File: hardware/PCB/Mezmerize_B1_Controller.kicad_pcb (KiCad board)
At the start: 2 copper layers, 100 x 70.9 mm, 51 parts, among them J1 230 Vac, J10 I2C DISPLAY (OLED/LCD), J11 I2C (FUTURE USE), J12 ROTARY ENC & SWITCH (FUTURE U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, J13 ROTARY ENC & SWITCH, J14 IR RECV, J2 B1 Relays, J3 PWR AMP L 12V TRIGGER, J4 PWR AMP L SWITCH, J5 PWR AMP R 12V TRIGGER, J6 PWR AMP R SWITCH, J7 PWR AMP TEMP NTC L, J8 PWR AMP TEMP NTC R, J9 MUSES 72320 (SPI), U1 AGQ20T03, U2 AGQ20T03, U3 ULN2803ADWR, U4 L7808CV, U5 MCP23008-E_SO, U6 24C02C_SN, U8 ESP32-DEVKIT-V1

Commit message: schenatics + symbols
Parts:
- moved U8 25.5 mm to (116.8, 172.7), turned to -90 degrees

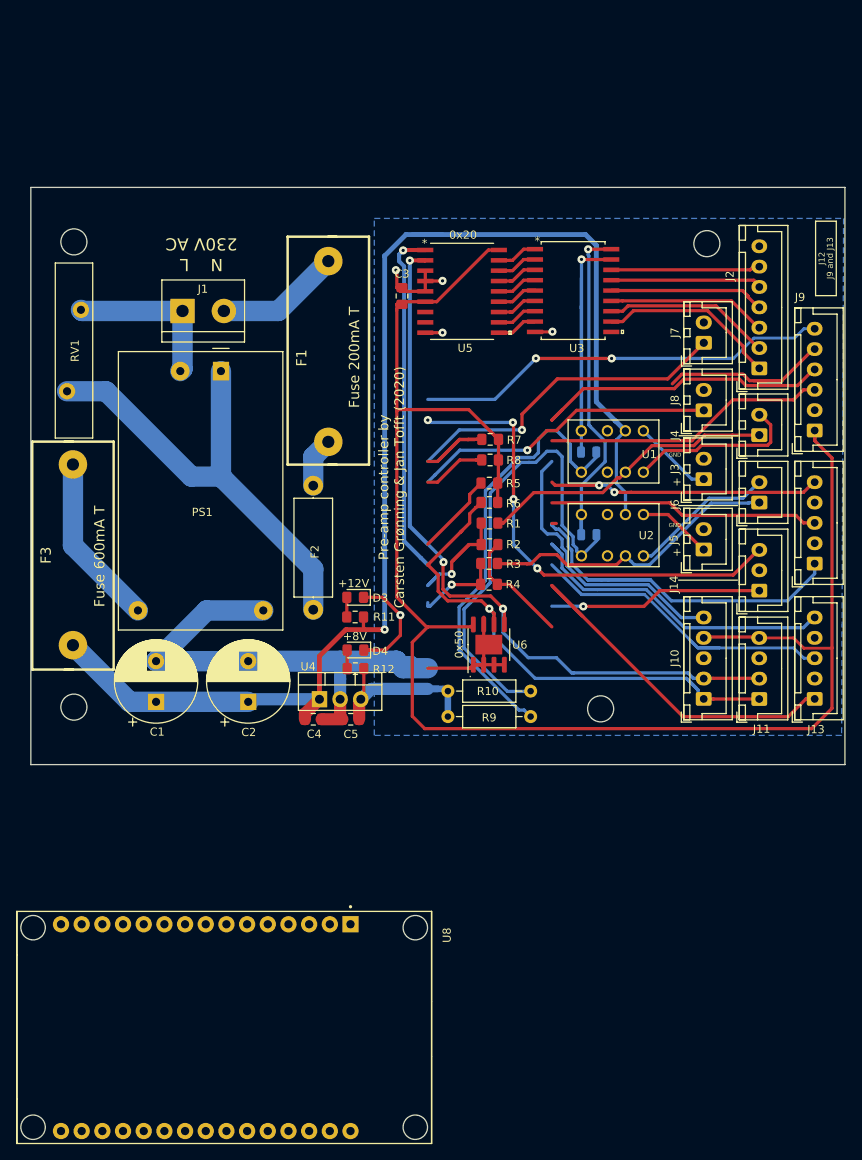
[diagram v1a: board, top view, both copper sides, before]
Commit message: PCB split
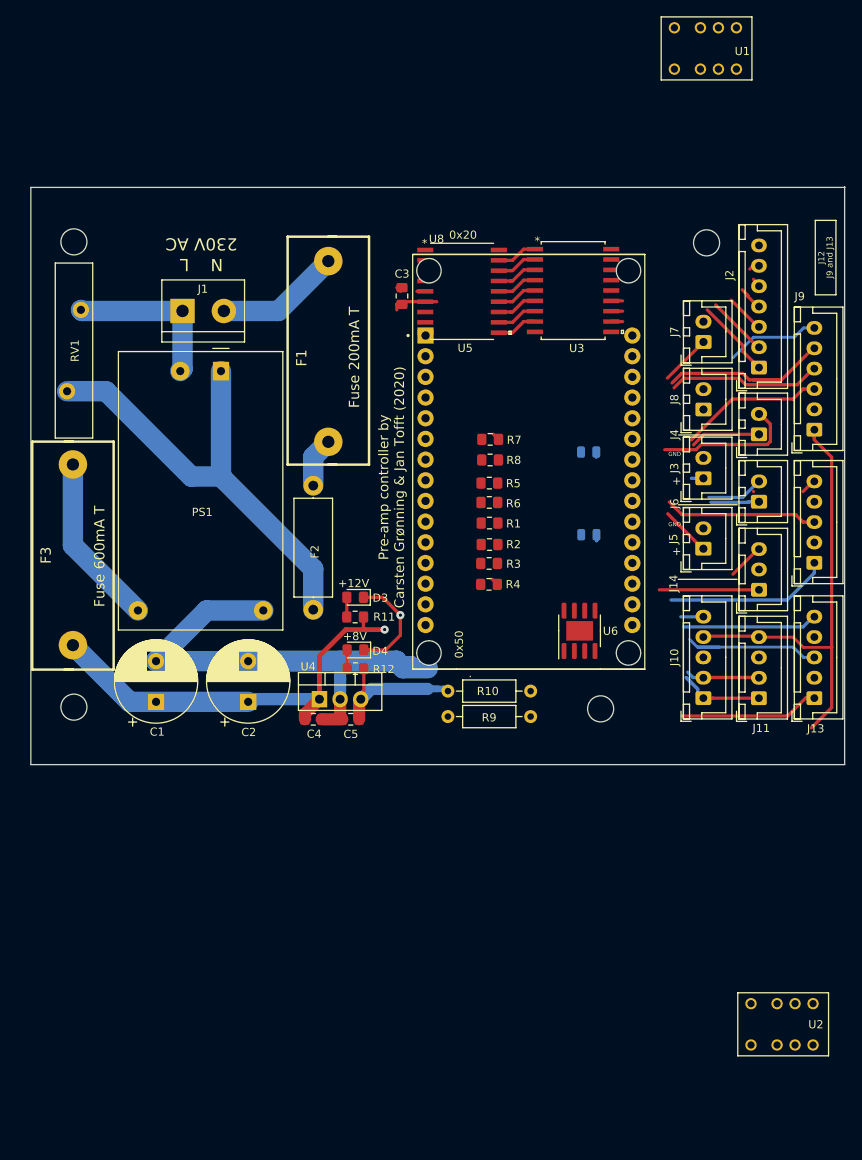
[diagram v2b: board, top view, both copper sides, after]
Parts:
- moved U8 78.9 mm to (154.3, 103.2), turned to 0 degrees
- moved U2 63.6 mm to (189.4, 169.8)
- moved U1 50.8 mm to (180.0, 49.9)
- moved U6 11.3 mm to (160.5, 124.0)
- moved J3 0.11 mm to (175.7, 105.2)
- moved J14 0.11 mm to (182.5, 118.9)
- moved J9 0.11 mm to (189.3, 99.3)
- moved REF** 0.11 mm to (176.1, 76.3)
- moved J10 0.11 mm to (175.7, 132.2)
- moved J5 0.11 mm to (175.7, 113.9)
- moved J11 0.11 mm to (182.5, 132.2)
- moved J12 0.11 mm to (189.3, 115.6)
- moved J13 0.11 mm to (189.3, 132.2)
- moved J2 0.11 mm to (182.5, 91.6)
- moved J4 0.11 mm to (182.5, 99.8)
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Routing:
- net +3V3: track 262.4 -> 67.2 mm, vias 4 -> 0
- net +12V: track 166.3 -> 53.2 mm
- net I2C:SCL: track 108.6 -> 12.0 mm, vias 2 -> 0
- net I2C:SDA: track 101.5 -> 9.18 mm, vias 3 -> 0
- net Net-(D1-Pad1): track 62.7 -> 0.63 mm
- net Net-(D2-Pad1): track 58.9 -> 1.38 mm
- net NTC_L: track 56.9 -> 6.26 mm, vias 1 -> 0
- net Net-(D1-Pad2): track 46.4 -> 0.05 mm, vias 1 -> 0
- net NTC_R: track 69.4 -> 24.1 mm, vias 1 -> 0
- net GND: track 160.5 -> 115.8 mm, vias 5 -> 1
- net Net-(D2-Pad2): track 42.5 -> 0.13 mm, vias 1 -> 0
- net Net-(J9-Pad6): track 51.1 -> 11.5 mm, vias 2 -> 0
- net Net-(U8-Pad22): track 34.7 -> 2.70 mm
- net Net-(J6-Pad1): track 38.1 -> 6.22 mm
- net Net-(U8-Pad23): track 33.5 -> 1.91 mm, vias 2 -> 0
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- removed copper zone on B.Cu, net GND
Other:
- board size 100 x 70.9 mm -> 100 x 71 mm

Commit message: Missing changes ??
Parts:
- removed the C1 at (108.5, 132.7)
- removed C2: 470uF, Capacitor_THT:CP_Radial_D10.0mm_P5.00mm
- removed C4: 0.33uF, Capacitor_SMD:C_0805_2012Metric_Pad1.15x1.40mm_HandSolder
- removed C5: 0.1uF, Capacitor_SMD:C_0805_2012Metric_Pad1.15x1.40mm_HandSolder
- removed D3, D4: LED, LED_SMD:LED_0805_2012Metric_Pad1.15x1.40mm_HandSolder
- removed F1: Fuse 200mA T, B1 Mezmerize Controller:BLX-A
- removed F2: Thermal fuse 73dgr, Resistor_THT:R_Axial_DIN0414_L11.9mm_D4.5mm_P15.24mm_Horizontal
- removed F3: Fuse 600mA T, B1 Mezmerize Controller:BLX-A
- removed the J1 at (111.7, 84.7)
- removed PS1: HLK-PM12, Converter_ACDC:Converter_ACDC_HiLink_HLK-PMxx
- removed the R1 at (149.4, 110.7)
- removed R11, R12: 4K7, Resistor_SMD:R_0805_2012Metric_Pad1.15x1.40mm_HandSolder
- removed R2: 5K, Resistor_SMD:R_0805_2012Metric_Pad1.15x1.40mm_HandSolder
- removed R3: 10K, Resistor_SMD:R_0805_2012Metric_Pad1.15x1.40mm_HandSolder
- removed the R4 at (149.4, 118.3)
- removed REF** (x4): MountingHole_3.2mm_M3_ISO7380, MountingHole:MountingHole_3.2mm_M3_ISO7380
- removed RV1: Varistor, Varistor:RV_Disc_D21.5mm_W4.6mm_P10mm
- removed the U4 at (128.5, 132.4)
- removed U8: ESP32-DEVKIT-V1, Dev Kit 1 - esp32:MODULE_ESP32_DEVKIT_V1
- added J14: 12V, TerminalBlock:TerminalBlock_bornier-2_P5.08mm, F.Cu at (175.8, 120.4)
- added J15: 8V, TerminalBlock:TerminalBlock_bornier-2_P5.08mm, F.Cu at (175.8, 108.9)
- added U6: ESP32-DEVKIT-V1, ESP32FP:MODULE_ESP32_DEVKIT_V1, F.Cu at (230.4, 114.1)
- D1, D2: moved to F.Cu
- J11: renamed from J12; value ROTARY ENC & SWITCH (FUTURE USE) -> ROTARY ENC & SWITCH 1
- J12: renamed from J13; value ROTARY ENC & SWITCH -> ROTARY ENC & SWITCH 2
- moved R7 103.8 mm to (252.6, 112.6)
- moved R9 103.8 mm to (252.4, 121.5), turned to 180 degrees
- moved R8 102.6 mm to (252.0, 106.4)
- moved C1 99.4 mm to (233.2, 113.6), turned to -90 degrees
- moved J6 93.3 mm to (262.3, 123.3), turned to -90 degrees
- moved J7 87.9 mm to (261.9, 113.9), turned to -90 degrees
- moved U4 85.9 mm to (225.8, 114.2), turned to 180 degrees
- moved R10 84.5 mm to (233.9, 106.5), turned to 180 degrees
- moved U5 83.7 mm to (243.5, 113.6), turned to -90 degrees
- moved J13 81.2 mm to (262.0, 102.2), turned to -90 degrees
- moved J9 77.5 mm to (253.2, 133.8), turned to 180 degrees
- moved U1 76.4 mm to (188.4, 125.8), turned to 0 degrees
- moved U2 69.2 mm to (183.2, 100.9), turned to 180 degrees
- moved U3 61.5 mm to (212.1, 114.3), turned to 180 degrees
- moved R1 59.5 mm to (201.5, 117.9), turned to 180 degrees
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- renumbered C3 to C1, J2 to J1, J11 to J10, J14 to J13, J3 to J2, J4 to J3, J5 to J4, J6 to J5, J7 to J6, J8 to J7, J9 to J8, J10 to J9, R9 to R1, R5 to R10, R10 to R4, R6 to R9, U5 to U4, U6 to U5
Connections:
- J11 pad 1: Net-(U8-Pad25) -> SW_1
- J11 pad 3: Net-(U8-Pad24) -> CCW_1
- J11 pad 5: Net-(U8-Pad23) -> CW_1
- J12 pad 1: Net-(J13-Pad1) -> SW_2
- J12 pad 3: Net-(J13-Pad3) -> CCW_2
- J12 pad 5: Net-(J13-Pad5) -> CW_2
- J13 pad 1: Net-(J14-Pad1) -> IR OUT
- J8 pad 3: Net-(J9-Pad3) -> SPI:SS
- J8 pad 4: Net-(J9-Pad4) -> SPI:MOSI
- J8 pad 5: NTC_R -> SPI:MISO
- J8 pad 6: Net-(J9-Pad6) -> SPI:SCK
- J9 pad 5: Net-(U8-Pad22) -> CONTRAST(LCD)
- R9 pad 1: I2C:SCL -> SPI:MOSI
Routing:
- net GND: track 115.8 -> 1.67 mm, vias 1 -> 0
- net Net-(F1-Pad2): track 64.6 -> 0.00 mm
- net +3V3: track 67.2 -> 5.71 mm
- net +12V: track 53.2 -> 0.00 mm, vias 1 -> 0
- net NTC_R: track 24.1 -> 0.00 mm
- net Net-(F3-Pad2): track 21.2 -> 0.00 mm
- net Net-(U8-Pad25): track 20.2 -> 0.00 mm
- net Net-(J1-Pad1) (its old number): track 20.0 -> 0.00 mm
- net Net-(J9-Pad4): track 19.0 -> 0.00 mm
- net +8V: track 18.9 -> 0.00 mm
- net Net-(J13-Pad3): track 18.9 -> 0.00 mm
- net Net-(U8-Pad24): track 18.8 -> 0.00 mm
- net Net-(J9-Pad3): track 17.7 -> 0.00 mm
- net Net-(J3-Pad2): track 17.4 -> 0.00 mm
- net Net-(J13-Pad1): track 17.1 -> 0.00 mm
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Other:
- board outline removed
- board text removed: "+"
- board text removed: "+12V"
- board text removed: "+8V"
- board text removed: "."
- board text removed: "0x50"
- board text removed: "230V AC"
- board text removed: "GND"
- board text removed: "J9 and J13"
- board text removed: "N L"

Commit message: mod psu + control v 0.25
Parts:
- added REF**: MountingHole_3.2mm_M3_ISO7380, MountingHole:MountingHole_3.2mm_M3_ISO7380, F.Cu at (125.0, 55.0)
- added REF**: MountingHole_3.2mm_M3_ISO7380, MountingHole:MountingHole_3.2mm_M3_ISO7380, F.Cu at (175.0, 145.0)
- added REF**: MountingHole_3.2mm_M3_ISO7380, MountingHole:MountingHole_3.2mm_M3_ISO7380, F.Cu at (175.0, 55.0)
- added REF**: MountingHole_3.2mm_M3_ISO7380, MountingHole:MountingHole_3.2mm_M3_ISO7380, F.Cu at (125.0, 145.0)
- moved J6 124.4 mm to (139.9, 145.5), turned to 180 degrees
- moved J9 123.9 mm to (129.3, 136.4), turned to 90 degrees
- moved J7 116.9 mm to (149.3, 145.1), turned to 180 degrees
- moved R9 111.6 mm to (141.7, 135.6), turned to 90 degrees
- moved J13 109.8 mm to (161.0, 145.2), turned to 180 degrees
- moved J8 108.1 mm to (129.3, 119.8), turned to 90 degrees
- moved R7 104.7 mm to (150.6, 135.8), turned to 90 degrees
- moved R8 99.5 mm to (156.8, 135.2), turned to -90 degrees
- moved U5 94.8 mm to (149.6, 126.7), turned to 180 degrees
- moved J10 93.9 mm to (128.8, 99.1), turned to 90 degrees
- moved J3 91.1 mm to (125.0, 65.5), turned to 90 degrees
- moved J2 90.9 mm to (125.0, 75.5), turned to 90 degrees
- moved C1 83.6 mm to (149.6, 116.4), turned to 180 degrees
- moved U6 81.3 mm to (149.1, 113.6), turned to 0 degrees
- moved J11 80.8 mm to (169.2, 126.4), turned to -90 degrees
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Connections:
- J14 pad 1: GND -> +12V
- J14 pad 2: +12V -> GND
- J15 pad 1: GND -> +8V
- J15 pad 2: +8V -> GND
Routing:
- net +12V: track 0.00 -> 67.7 mm
- net +8V: track 0.00 -> 52.0 mm
- net Net-(J3-Pad1): track 0.00 -> 17.0 mm
- net Net-(J4-Pad1): track 0.00 -> 16.6 mm
- net Net-(J3-Pad2): track 0.00 -> 14.4 mm
- net Net-(J5-Pad1): track 0.00 -> 13.7 mm
- net Net-(J5-Pad2): track 0.00 -> 9.76 mm
- net Net-(J2-Pad1): track 0.00 -> 9.76 mm
- net Net-(D2-Pad1): track 0.00 -> 8.58 mm
- net Net-(D1-Pad1): track 0.00 -> 6.72 mm
- net Net-(D2-Pad2): track 0.00 -> 3.94 mm
- net Net-(D1-Pad2): track 0.00 -> 3.74 mm
- net Net-(J1-Pad3): track 1.39 -> 0.00 mm
- net Net-(J1-Pad2): track 1.39 -> 0.00 mm
- net Net-(J1-Pad1): track 1.39 -> 0.00 mm
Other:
- board outline added: 60 x 100 mm

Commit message: updated pcb
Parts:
- moved J8 10.6 mm to (125.0, 110.0)
- moved R7 10.4 mm to (153.8, 126.0)
- moved J9 10.2 mm to (125.0, 127.2)
- moved R9 10.1 mm to (144.8, 126.0), turned to -90 degrees
- moved J10 9.53 mm to (125.0, 90.3)
- moved R8 9.30 mm to (158.0, 126.0)
- moved U5 7.39 mm to (150.6, 119.4)
- moved J11 7.30 mm to (175.0, 122.0)
- moved J1 7.28 mm to (175.0, 82.7)
- moved J12 6.99 mm to (175.0, 104.8)
- moved R10 6.50 mm to (150.6, 114.8), turned to 0 degrees
- moved J13 4.36 mm to (162.6, 141.2)
- moved C1 4.34 mm to (150.6, 112.2)
- moved U3 4.34 mm to (149.9, 91.1)
- moved U4 4.34 mm to (150.0, 104.8)
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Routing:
- net +3V3: track 5.71 -> 138.4 mm
- net CONTRAST(LCD): track 0.00 -> 98.9 mm
- net I2C:SDA: track 0.16 -> 78.6 mm, vias 0 -> 3
- net I2C:SCL: track 0.06 -> 76.1 mm, vias 0 -> 1
- net NTC_L: track 0.00 -> 65.6 mm
- net SPI:MOSI: track 0.00 -> 53.7 mm
- net IR OUT: track 0.00 -> 35.0 mm
- net NTC_R: track 0.00 -> 32.4 mm
- net Net-(J1-Pad6): track 0.00 -> 32.0 mm
- net Net-(J1-Pad5): track 0.00 -> 29.7 mm
- net CW_1: track 0.00 -> 27.8 mm
- net Net-(J1-Pad4): track 0.00 -> 27.4 mm
- net Net-(J1-Pad2): track 0.00 -> 26.7 mm
- net Net-(J1-Pad3): track 0.00 -> 26.5 mm
- net SPI:MISO: track 0.00 -> 26.1 mm
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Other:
- outline, holes or cut-outs redrawn

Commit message: Opdater print
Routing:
- net +3V3: track 138.4 -> 150.7 mm
- net GND: vias 0 -> 2
- added copper zone on B.Cu, net GND
- added copper zone on F.Cu, net GND
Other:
- board size 60 x 100 mm -> 60 x 95.8 mm
- board text added: "Pre-amp controller by Carsten Grønning & Jan Tofft (2022)"
- board text removed: "Pre-amp controller by Carsten Grønning & Jan Tofft (2020)"
